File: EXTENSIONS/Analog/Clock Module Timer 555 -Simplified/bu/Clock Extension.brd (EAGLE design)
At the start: 48 x 38 mm, 12 parts, among them Q1 2N3906, T555_CLOCK NE555N, X1 USB-A

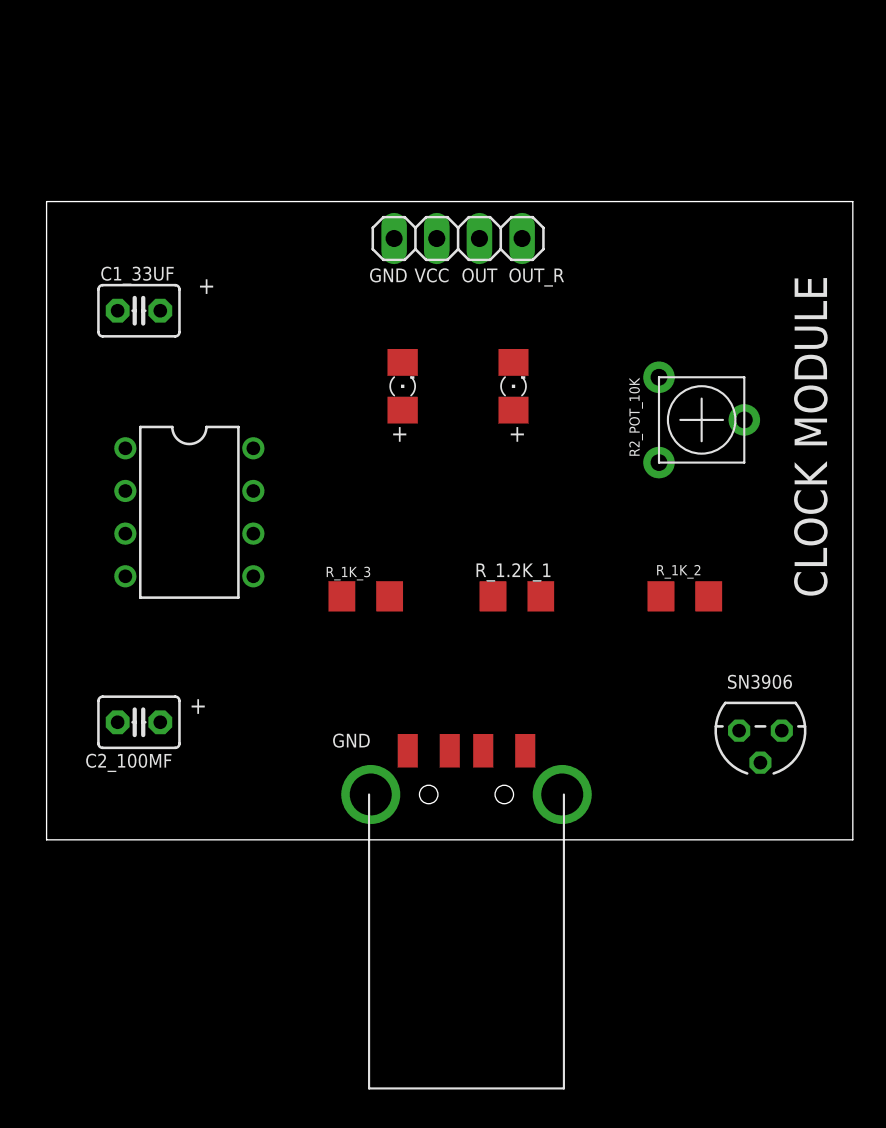
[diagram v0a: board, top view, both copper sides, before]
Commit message: Update/create Clock Module Time 555 -Simplified
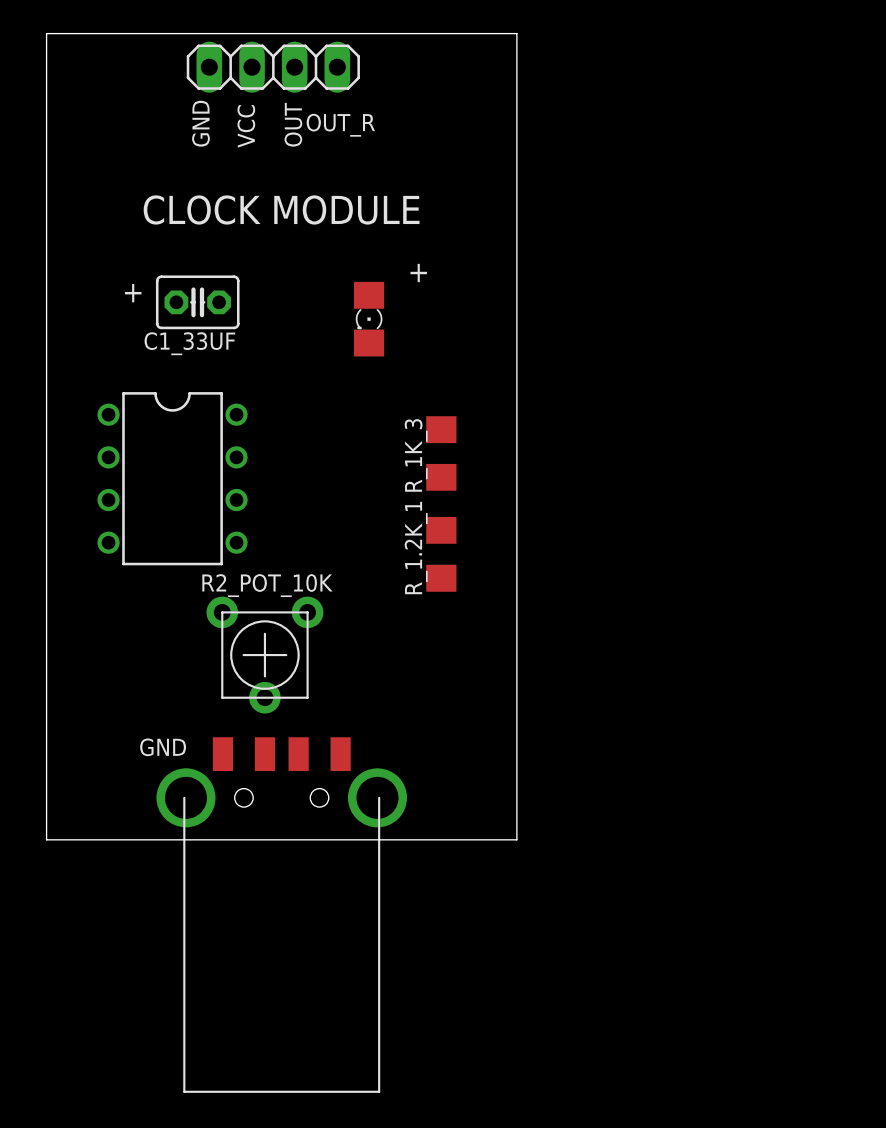
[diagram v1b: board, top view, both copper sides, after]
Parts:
- removed C2_100MF: (no value), adafruit:C025-030X050
- removed LED_OUTPUT_REVERSE: (no value), adafruit:1206
- removed Q1: 2N3906, transistor-pnp:TO92
- removed R_1K_2: (no value), adafruit:R1206
- moved R2_POT_10K 29.5 mm to (15.0, 23.0), turned to 180 degrees
- moved JP1 15.0 mm to (15.5, 58.0)
- moved X1 11.0 mm to (16.0, 14.5)
- moved R_1K_3 9.62 mm to (25.5, 35.0), turned to 90 degrees
- moved R_1.2K_1 5.15 mm to (25.5, 29.0), turned to 90 degrees
- moved LED_OUTPUT 4.47 mm to (21.2, 43.0), turned to 270 degrees
- moved C1_33UF 3.54 mm to (11.0, 44.0), turned to 180 degrees
- moved T555_CLOCK 2.24 mm to (9.50, 33.5)
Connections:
- removed net N$6: LED_OUTPUT_REVERSE.C, R_1K_2.2
- net GND: no longer C2_100MF.1
- net TMR555_OUTPUT: no longer Q1.2
- net TMR555_OUTPUT_REVERSE: no longer Q1.3, R_1K_2.1
- net VCC: no longer C2_100MF.2, LED_OUTPUT_REVERSE.A
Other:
- board size 48 x 38 mm -> 28 x 48 mm
- board text removed: "SN3906"

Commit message: Update/create Clock Module Time 555 -Simplified
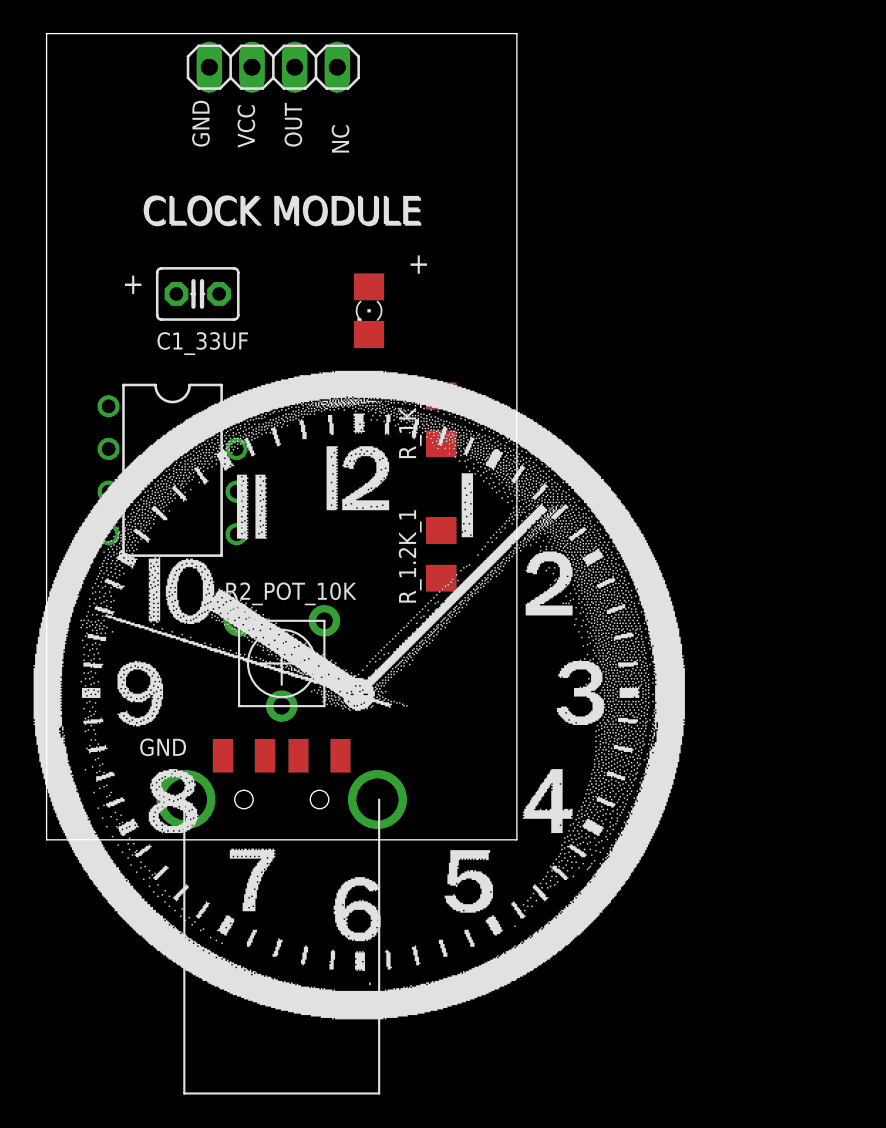
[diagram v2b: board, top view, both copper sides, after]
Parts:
- moved R_1K_3 2.00 mm to (25.5, 37.0)
- moved R2_POT_10K 1.12 mm to (16.0, 22.5)
- moved C1_33UF 0.50 mm to (11.0, 44.5)
- moved LED_OUTPUT 0.50 mm to (21.2, 43.5)
- moved T555_CLOCK 0.50 mm to (9.50, 34.0)
- moved X1 0.10 mm to (16.0, 14.4)
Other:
- board text added: "NC"
- board text added: "PCBv3 - 2019.08"
- board text removed: "OUT_R"
- board text removed: "PCBv2 - 2017.08"

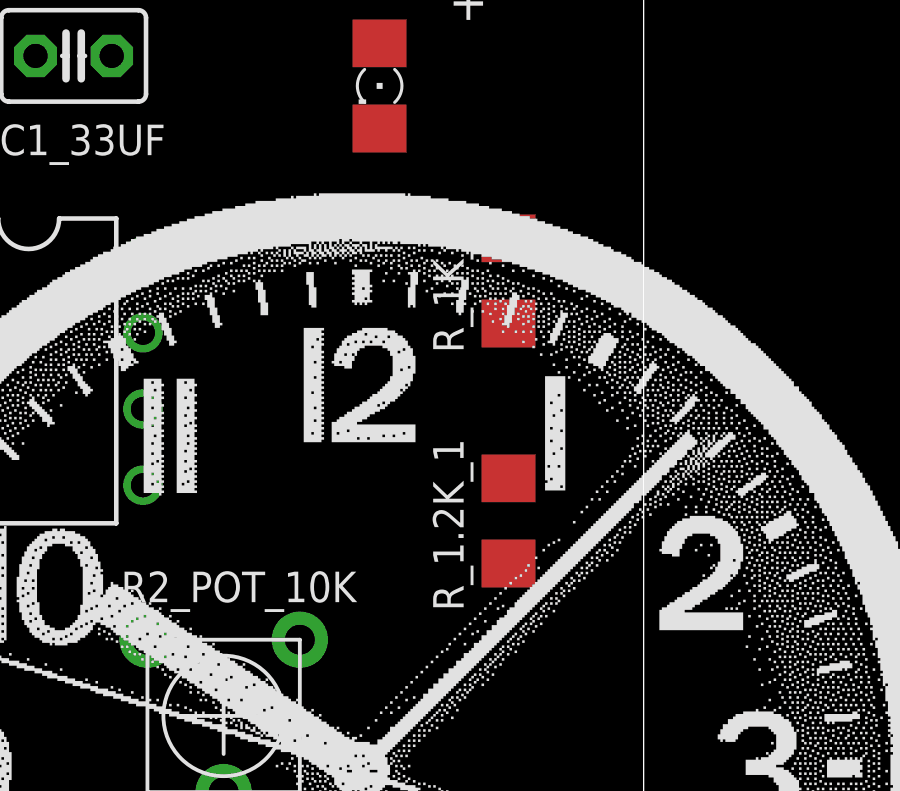
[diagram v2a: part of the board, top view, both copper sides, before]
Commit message: Update/create Clock Module Time 555 -Simplified
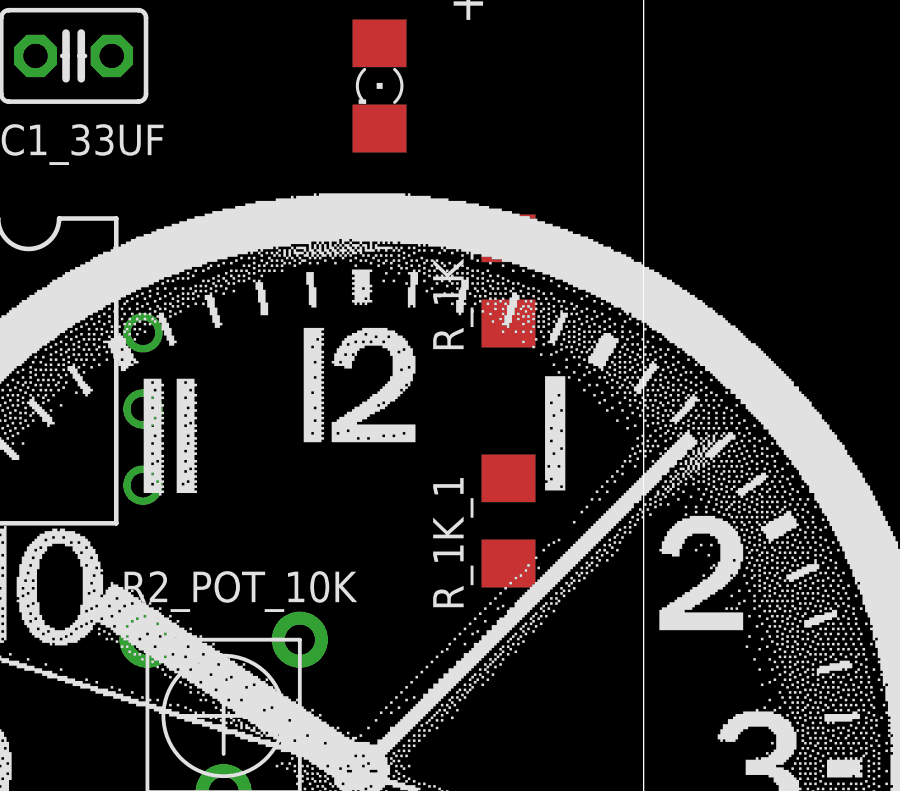
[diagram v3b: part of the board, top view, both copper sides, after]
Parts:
- renumbered R_1.2K_1 to R_1K_1, R_1K_3 to R_1K_2
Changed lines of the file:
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@@
 <attribute name="VALUE" x="10.42" y="54.825" size="1.27" layer="27"/>
 </element>
-<element name="R_1.2K_1" library="adafruit" package="R1206" value="" x="25.5" y="29" smashed="yes" rot="R90">
+<element name="R_1K_1" library="adafruit" package="R1206" value="" x="25.5" y="29" smashed="yes" rot="R90">
 <attribute name="NAME" x="24" y="26" size="1.016" layer="25" rot="R90"/>
 <attribute name="VALUE" x="27.913" y="27.603" size="1.27" layer="27" rot="R90"/>
@@
 <attribute name="VALUE" x="18.66" y="44.77" size="1.27" layer="27" rot="R270"/>
 </element>
-<element name="R_1K_3" library="adafruit" package="R1206" value="" x="25.5" y="37" smashed="yes" rot="R90">
+<element name="R_1K_2" library="adafruit" package="R1206" value="" x="25.5" y="37" smashed="yes" rot="R90">
 <attribute name="NAME" x="24" y="34.603" size="1.016" layer="25" rot="R90"/>
 <attribute name="VALUE" x="27.913" y="35.603" size="1.27" layer="27" rot="R90"/>
@@
 <contactref element="C1_33UF" pad="1"/>
 <contactref element="JP1" pad="1"/>
-<contactref element="R_1K_3" pad="1"/>
+<contactref element="R_1K_2" pad="1"/>
 <wire x1="12.27" y1="44.5" x2="11.69" y2="58" width="0" layer="19" extent="1-1"/>
 <wire x1="5.69" y1="37.81" x2="12.27" y2="44.5" width="0" layer="19" extent="1-1"/>
@@
 <contactref element="T555_CLOCK" pad="4"/>
 <contactref element="JP1" pad="2"/>
-<contactref element="R_1.2K_1" pad="2"/>
+<contactref element="R_1K_1" pad="2"/>
 <wire x1="13.31" y1="37.81" x2="14.23" y2="58" width="0" layer="19" extent="1-1"/>
 <wire x1="5.69" y1="30.19" x2="13.31" y2="37.81" width="0" layer="19" extent="1-1"/>
@@
 <signal name="N$1">
 <contactref element="T555_CLOCK" pad="7"/>
-<contactref element="R_1.2K_1" pad="1"/>
+<contactref element="R_1K_1" pad="1"/>
 <contactref element="R2_POT_10K" pad="3"/>
 <wire x1="13.46" y1="25.04" x2="25.5" y2="27.578" width="0" layer="19" extent="1-1"/>
@@
 <signal name="N$5">
 <contactref element="LED_OUTPUT" pad="C"/>
-<contactref element="R_1K_3" pad="2"/>
+<contactref element="R_1K_2" pad="2"/>
 <wire x1="25.5" y1="38.422" x2="21.2" y2="42.078" width="0" layer="19" extent="1-1"/>
 </signal>

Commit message: Prepare for shipping to seeedstudio manufacturing
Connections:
- removed net TMR555_OUTPUT_REVERSE: JP1.4
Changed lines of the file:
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@@
 <wire x1="25.5" y1="38.422" x2="21.2" y2="42.078" width="0" layer="19" extent="1-1"/>
-</signal>
-<signal name="TMR555_OUTPUT_REVERSE">
-<contactref element="JP1" pad="4"/>
 </signal>
 </signals>

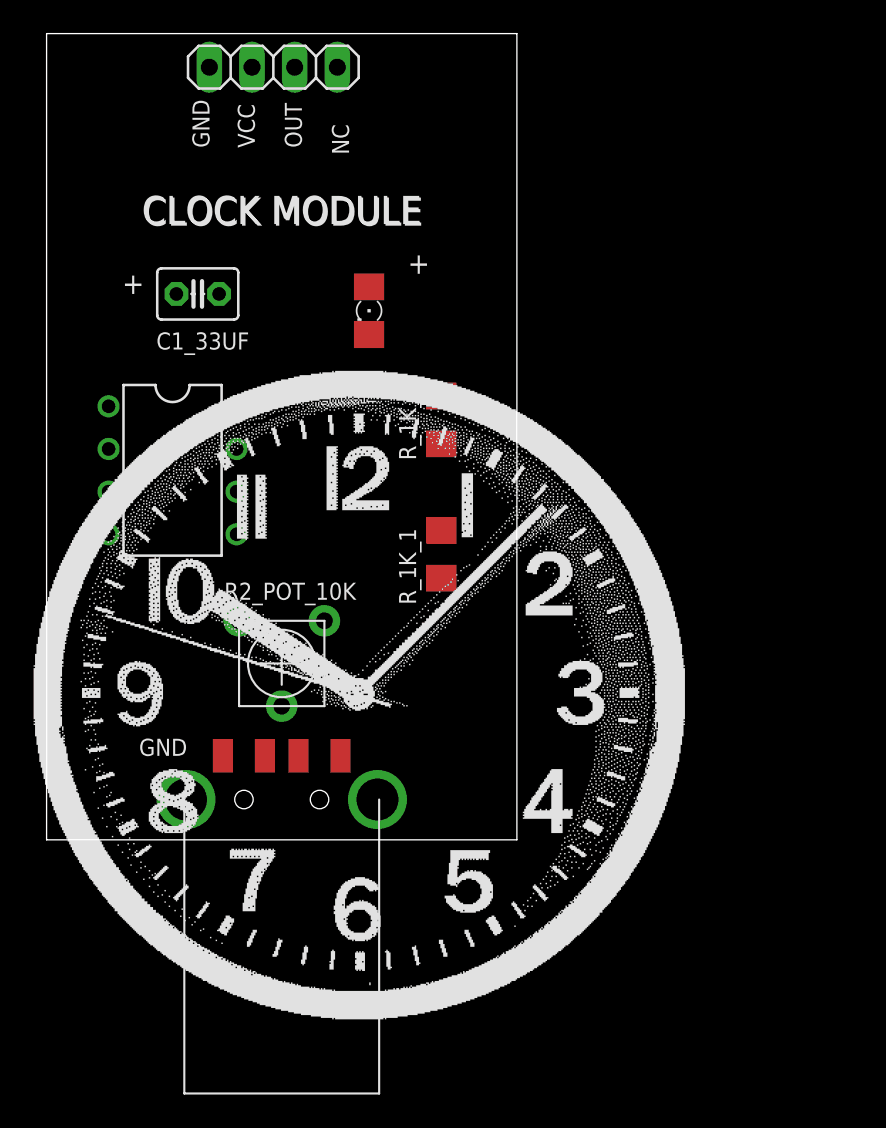
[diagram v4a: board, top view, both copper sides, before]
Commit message: fix bug in pcb '0 TO 9 Counter 74LS90'
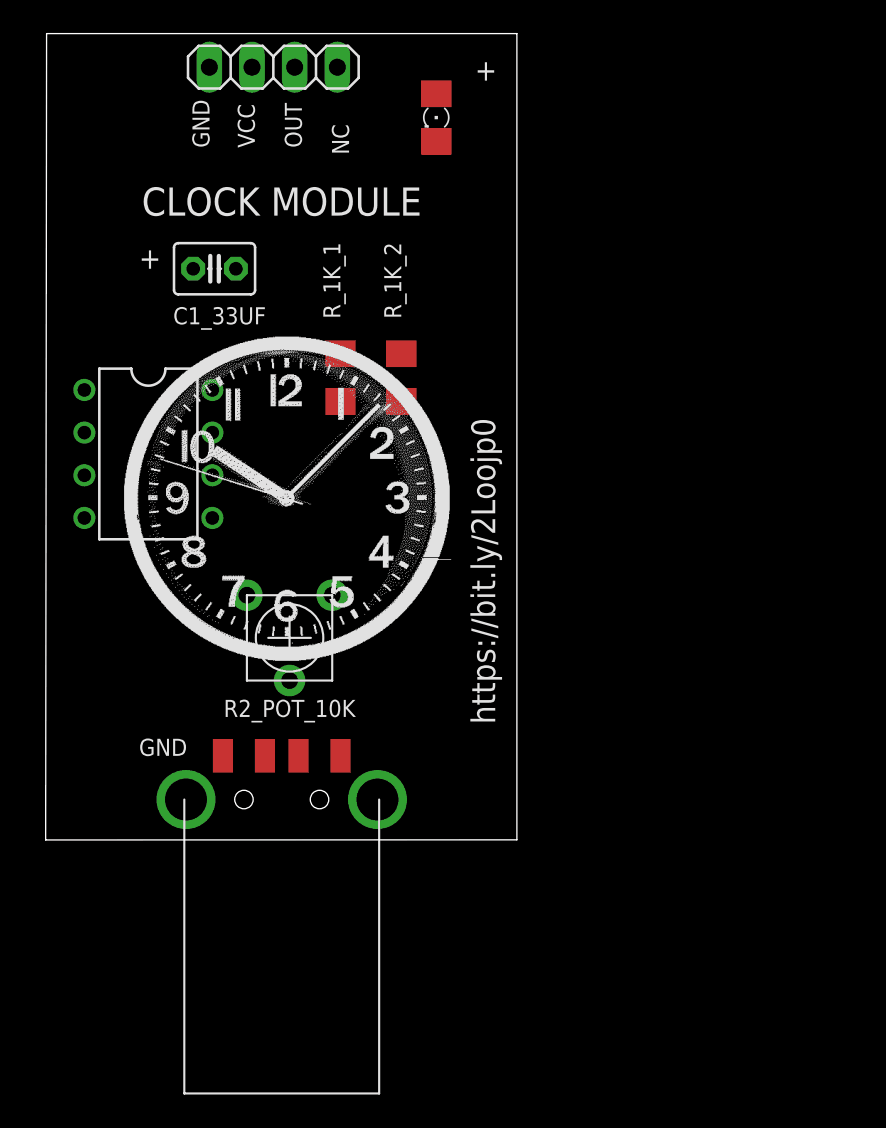
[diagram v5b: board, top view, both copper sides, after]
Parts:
- moved LED_OUTPUT 12.2 mm to (25.2, 55.0)
- moved R_1K_1 12.1 mm to (19.5, 39.5)
- moved R_1K_2 3.47 mm to (23.1, 39.5)
- moved C1_33UF 1.80 mm to (12.0, 46.0)
- moved T555_CLOCK 1.74 mm to (8.06, 35.0)
- moved R2_POT_10K 1.59 mm to (16.5, 24.0)
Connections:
- new net TMR555_OUTPUT_REVERSE: JP1.4
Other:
- board size 28 x 48 mm -> 28.1 x 48 mm
- board text added: "https://bit.ly/2Loojp0"
